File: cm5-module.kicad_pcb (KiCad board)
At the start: 4 copper layers, 100 x 100 mm, 263 parts, among them J1 DIN-41612-connector_090319679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, J10 HDMI-A_HDMI-19PIN-043, J11 USB-C_USB-310F-B-SU, J12 MicroSD_5033981892, J13 Programming connector, J14 Programming connector, J2 JST_SH_1x3_BM03B-SRSS-TB-LF-SN, J3 CM5_1-100_3mm-stack, J4 CM5_101-200_3mm-stack, J5 JST_SH_1x4_BM04B-SRSS-TB-LF-SN, J6 Bus_M.2_1-2199230-6, J7 RJ45_HC612601A-M893-A, J8 USB-A_USB-303WSD-BRY, J9 USB-C_TYPE-C_16PLT-H6.5, Q1 SIS472DN-T1-GE3, Q10 AO3401A, Q11 AO3400A, Q12 AO3400A, Q2 AO3400A, Q3 SIS472DN-T1-GE3, Q4 SIS472DN-T1-GE3, Q5 AO3401A, Q6 AO3401A, Q7 AO3400A, Q8 AO3400A, Q9 AO3401A, SW1 SW_TL2243, U1 LM74700QDBVRQ1, U10 LM74700QDBVRQ1, U11 AP22615AWU-7, U12 LM74700QDBVRQ1, U13 STM32G431CBU6, U14 TJA1044GTK_3Z, U15 STM32G431CBU6, U16 TJA1044GTK_3Z, U17 FSUSB42UMX, U2 AP22615AWU-7, U3 AP22615AWU-7, U4 AP22615AWU-7, U5 FT230XQ-R, U6 NTS0102DP, U7 CH334P, U8 SIC431AED-T1-GE3, U9 TPS564247DRLR, Y1 Oscillator_32.768kHz_OK2EL89C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, Y2 X322512MSB4SI

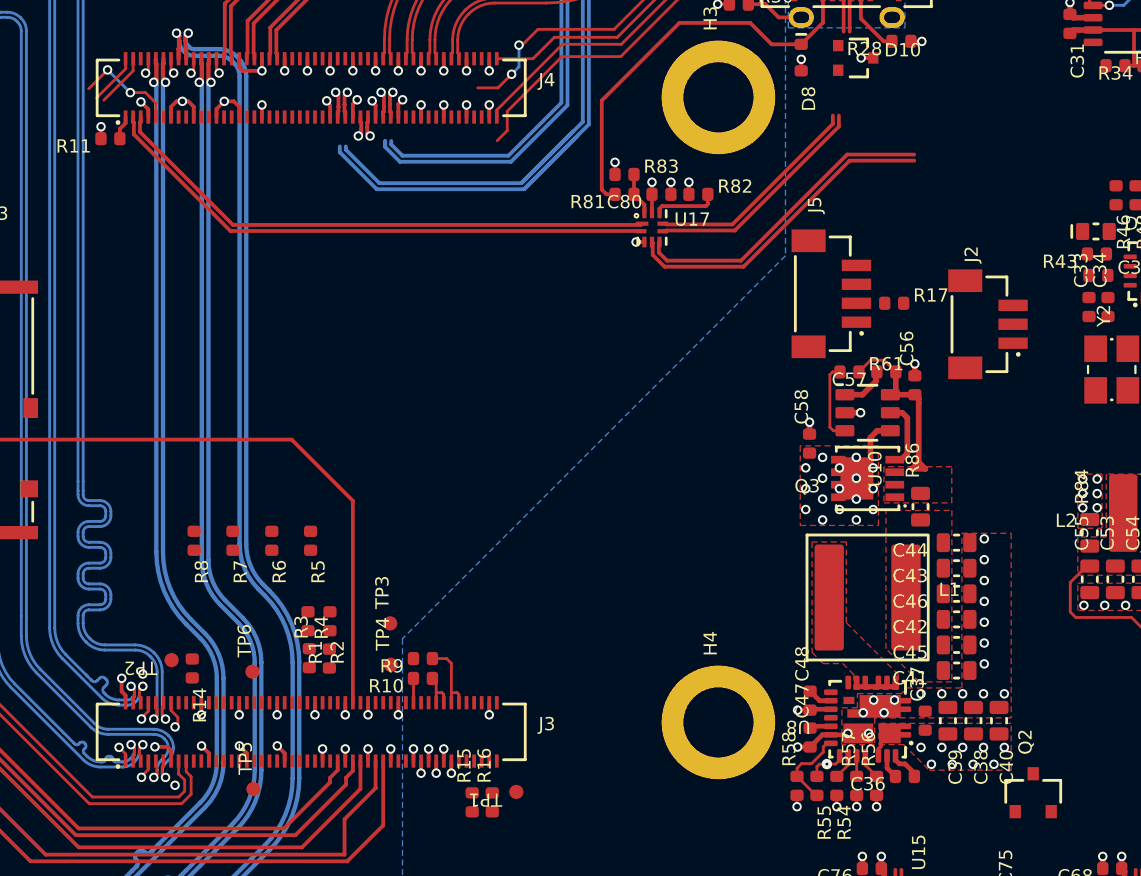
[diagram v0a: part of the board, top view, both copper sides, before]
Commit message: [#3] Move the 5V DC-DC ideal diode, position fan and debug JST connectors
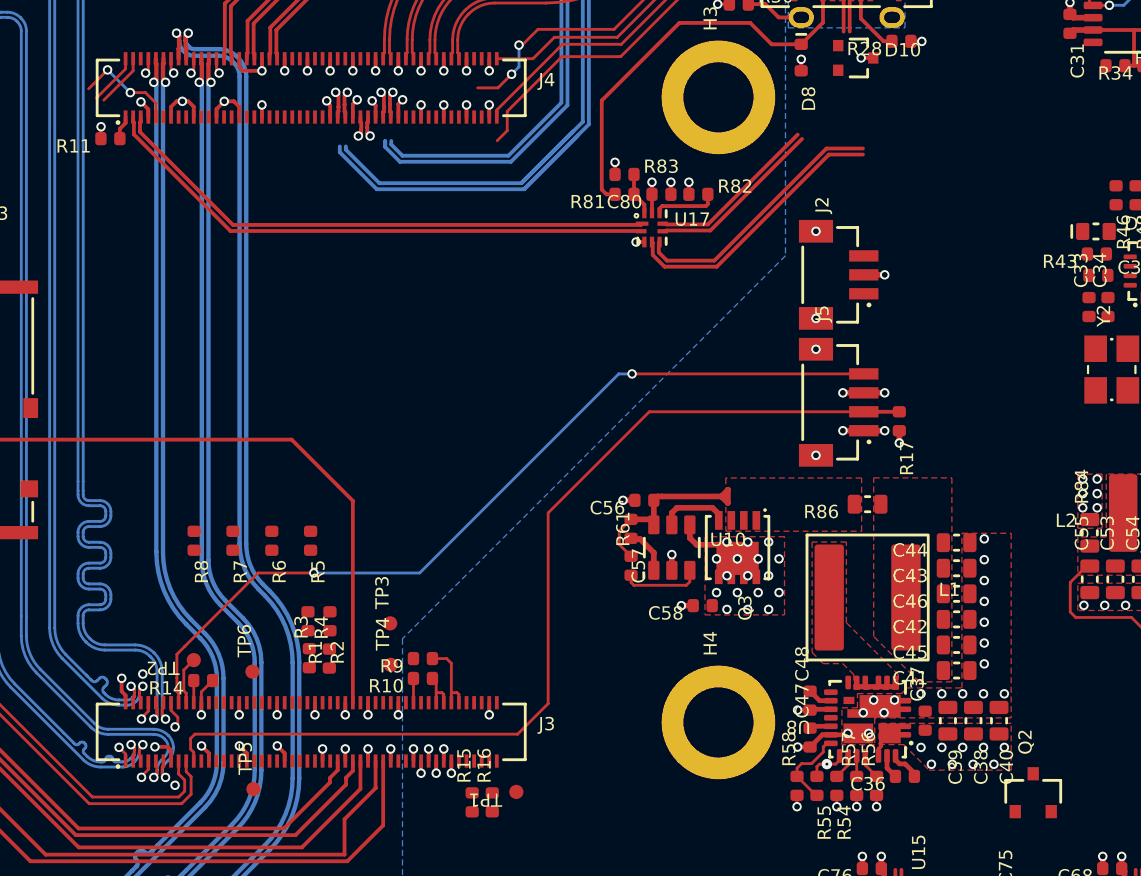
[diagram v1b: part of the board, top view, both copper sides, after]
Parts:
- moved C57 15.8 mm to (90.9, 100.3), turned to -90 degrees
- moved C56 15.5 mm to (91.6, 98.8), turned to 180 degrees
- moved R61 15.4 mm to (90.9, 102.3), turned to 90 degrees
- moved U10 12.6 mm to (93.1, 101.3), turned to 0 degrees
- moved C58 10.2 mm to (94.7, 104.4), turned to 180 degrees
- moved J2 8.30 mm to (101.5, 86.9)
- moved Q3 7.78 mm to (96.6, 101.3), turned to -90 degrees
- moved R17 6.24 mm to (105.1, 94.6), turned to -90 degrees
- moved J5 5.74 mm to (101.5, 93.7)
- moved R86 2.80 mm to (103.4, 99.0), turned to 180 degrees
- moved TP2 1.17 mm to (67.8, 107.3)
- moved R14 0.86 mm to (68.3, 108.3), turned to 180 degrees
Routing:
- net /CM5/FAN_PWM: track 0.00 -> 51.7 mm
- net /CM5/FAN_TACHO: track 0.00 -> 45.0 mm, vias 0 -> 2
- net GND: track 146.9 -> 151.6 mm, vias 204 -> 211
- net /USB switch/USB_2.D-: track 17.7 -> 14.9 mm
- net /USB hub/USB_HUB.D+: track 16.6 -> 14.0 mm
- net /USB hub/USB_HUB.D-: track 17.1 -> 14.5 mm
- net /USB switch/USB_2.D+: track 15.6 -> 13.1 mm
- net Net-(J3-Ethernet_SYNC_OUT): track 0.00 -> 2.52 mm
- net +5V: track 21.1 -> 23.3 mm, vias 50 -> 52
- net /CM5/~{EEPROM_WP}: track 0.00 -> 1.17 mm
- net +3V3: track 40.1 -> 40.8 mm, vias 21 -> 22

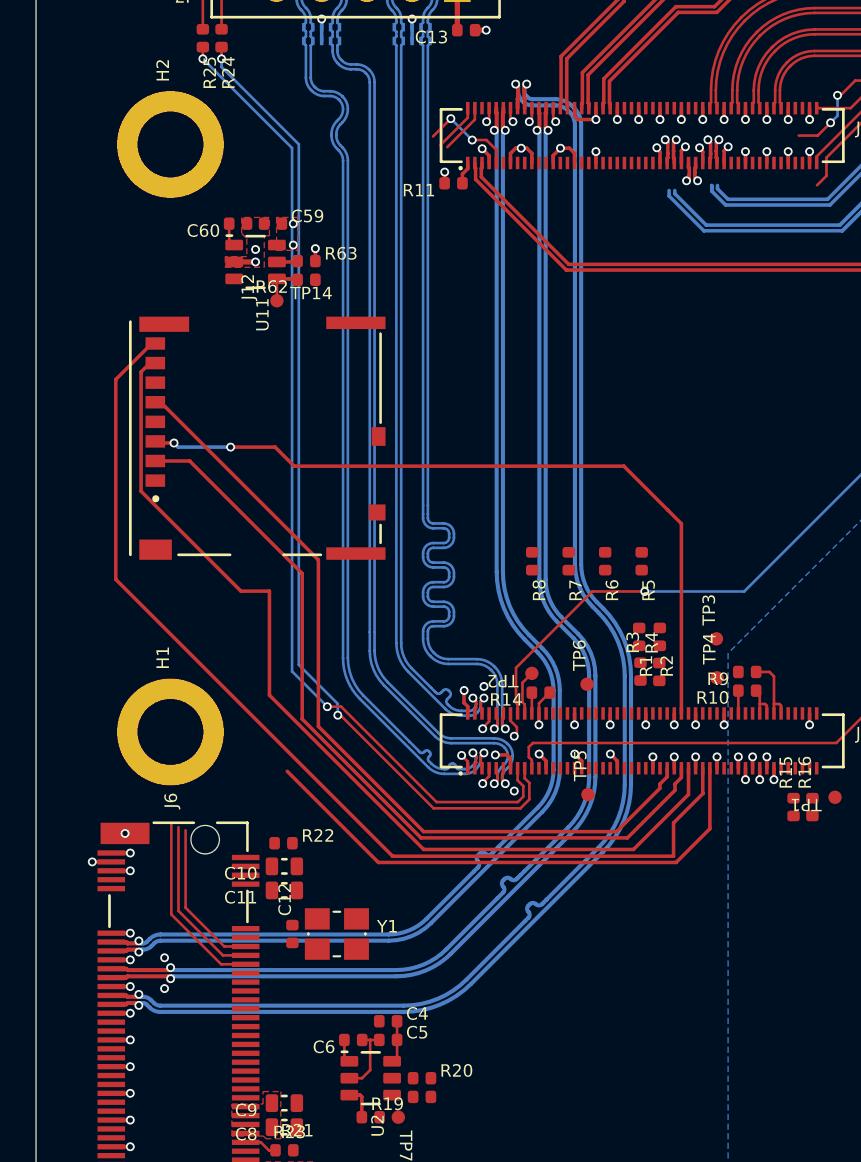
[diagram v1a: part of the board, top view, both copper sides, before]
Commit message: [#3] Layout SD card connector
NOTE: Used 0.3mm traces instead of 0.35mm ones on SDIO lines due to
limited space
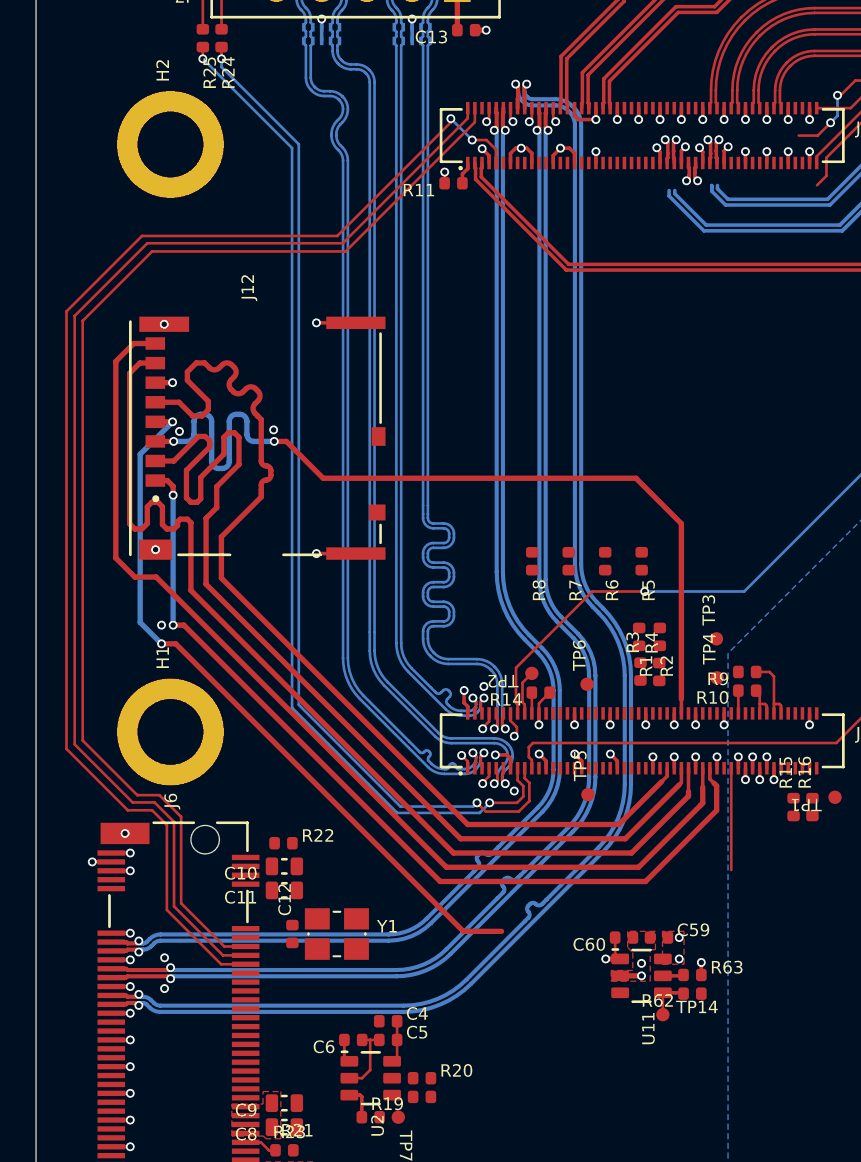
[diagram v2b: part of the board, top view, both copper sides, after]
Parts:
- moved R63 45.6 mm to (76.9, 124.2)
- moved TP14 45.6 mm to (75.2, 126.4)
- moved C60 45.6 mm to (73.0, 122.1)
- moved R62 45.6 mm to (76.9, 125.2)
- moved U11 45.6 mm to (74.0, 124.2)
- moved C59 45.6 mm to (75.0, 122.1)
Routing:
- net /CM5/~{PCIe_PERST}: track 15.9 -> 72.7 mm
- net /CM5/~{PCIe_CLKREQ}: track 12.2 -> 68.6 mm
- net /CM5/~{PCIe_WAKE}: track 11.5 -> 67.8 mm
- net /SD card/SD_+3V3: track 1.32 -> 42.6 mm, vias 0 -> 3
- net /CM5/SD_CARD.DAT2: track 30.0 -> 49.6 mm, vias 0 -> 2
- net /CM5/SD_CARD.DAT3: track 45.2 -> 57.2 mm
- net /CM5/SD_CARD.CLK: track 46.1 -> 57.0 mm
- net /CM5/SD_CARD.CMD: track 42.1 -> 49.8 mm
- net /CM5/SD_PWR_ON: track 0.00 -> 5.72 mm
- net GND: track 151.6 -> 157.0 mm, vias 211 -> 219
- net /CM5/SD_CARD.DAT0: track 53.0 -> 57.3 mm
- net /CM5/ETH.LED_ACT: track 55.0 -> 56.7 mm
- net /CM5/ETH.LED_LINK: track 55.2 -> 56.5 mm

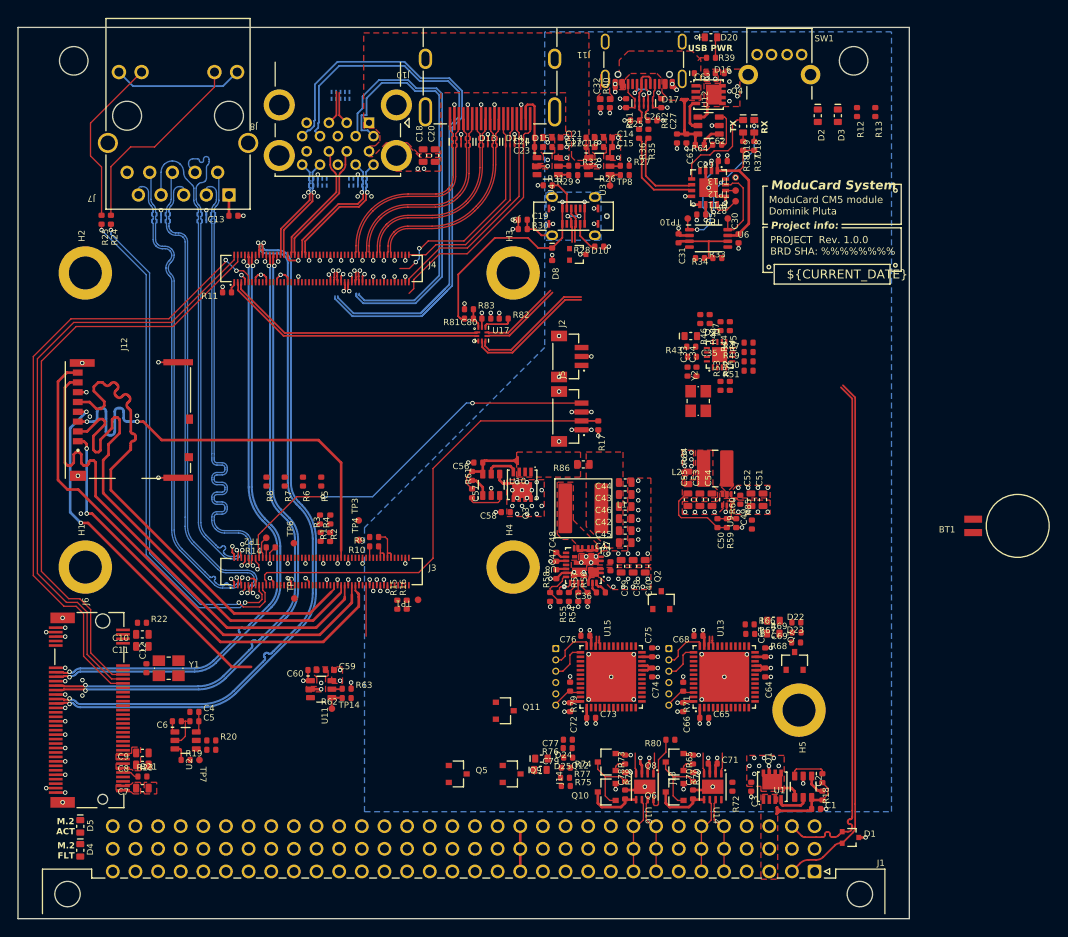
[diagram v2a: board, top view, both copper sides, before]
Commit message: [#3] Layout M.2 power
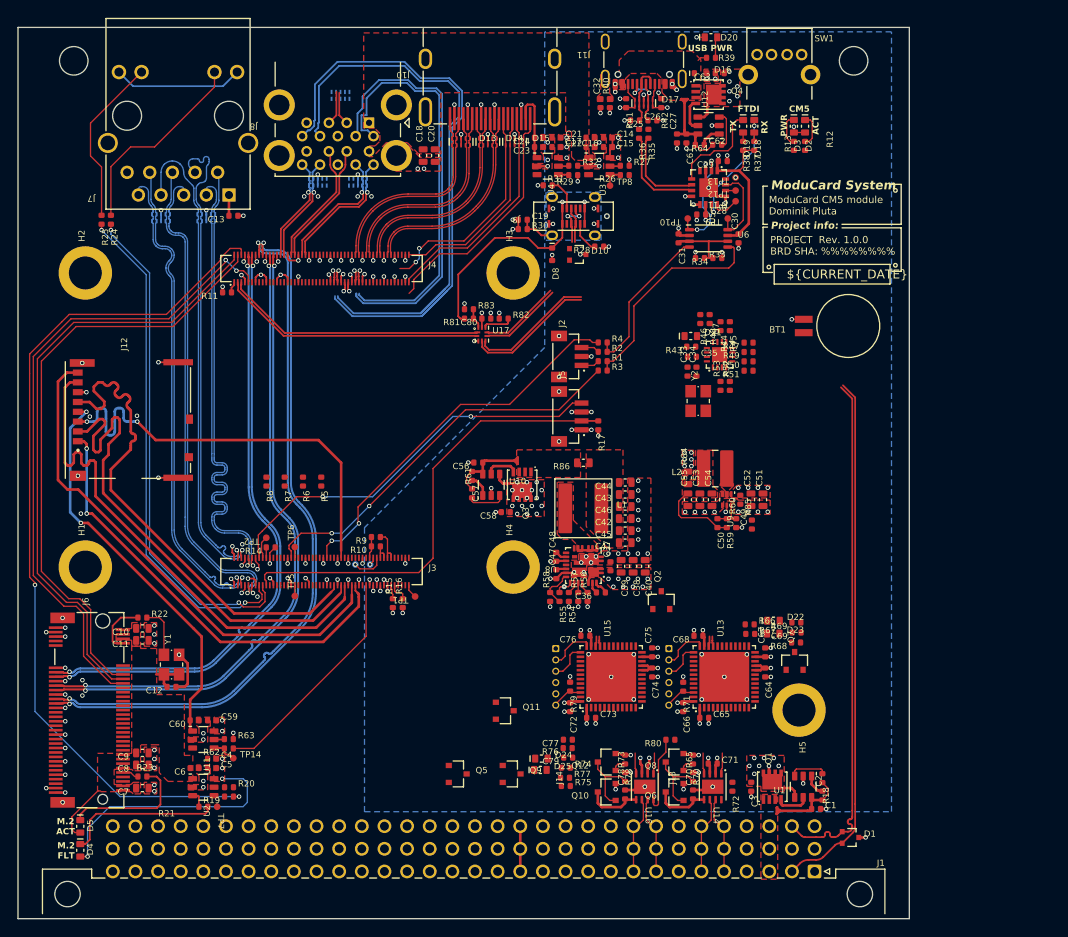
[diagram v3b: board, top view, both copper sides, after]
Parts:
- TP3, TP4: moved to B.Cu
- moved R4 37.6 mm to (105.6, 85.3), turned to 0 degrees
- moved R3 36.7 mm to (105.6, 88.5), turned to 0 degrees
- moved R1 36.4 mm to (105.6, 87.5), turned to 0 degrees
- moved R2 35.9 mm to (105.6, 86.4), turned to 0 degrees
- moved G*** 30.9 mm to (132.7, 79.8)
- moved REF** 30.9 mm to (128.3, 87.0)
- moved BT1 29.4 mm to (128.2, 83.5)
- moved R62 14.4 mm to (63.6, 130.9)
- moved U11 14.4 mm to (60.8, 129.9)
- moved C59 14.4 mm to (61.8, 127.8)
- moved C60 14.4 mm to (59.8, 127.8)
- moved R63 14.4 mm to (63.7, 129.8)
- moved TP14 12.4 mm to (64.1, 132.0)
- moved R13 9.89 mm to (127.0, 63.3), turned to 90 degrees
- moved R12 6.95 mm to (128.3, 63.3), turned to 90 degrees
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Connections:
- net Net-(BT1-+) renamed /CM5/VBAT
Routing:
- net /CM5/PCIe_PWR_EN: track 0.00 -> 97.3 mm, vias 0 -> 2
- net /CM5/UART2_RX: track 0.00 -> 44.3 mm, vias 0 -> 2
- net /CM5/UART2_TX: track 0.00 -> 42.7 mm, vias 0 -> 2
- net +3V3: track 40.8 -> 69.3 mm, vias 22 -> 28
- net /CM5/CONSOLE.TX: track 0.00 -> 24.6 mm
- net /CM5/SD_PWR_ON: track 5.72 -> 25.8 mm
- net Net-(D4-C): track 0.00 -> 17.6 mm
- net /CM5/CONSOLE.RX: track 0.00 -> 17.4 mm
- net Net-(D5-C): track 0.00 -> 14.5 mm
- net +3V3_M2: track 1.32 -> 11.0 mm
- net /M.2/SUSCLK_R: track 0.00 -> 6.22 mm
- net /M.2/SUSCLK: track 0.00 -> 5.79 mm
- net Net-(D2-C): track 0.00 -> 3.68 mm
- net Net-(D3-C): track 0.00 -> 3.66 mm
- net /CM5/SDA0: track 0.00 -> 3.61 mm, vias 0 -> 1
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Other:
- board text added: "ACT"
- board text added: "CM5"
- board text added: "FTDI"
- board text added: "PWR"

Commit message: [#3] Layout USB
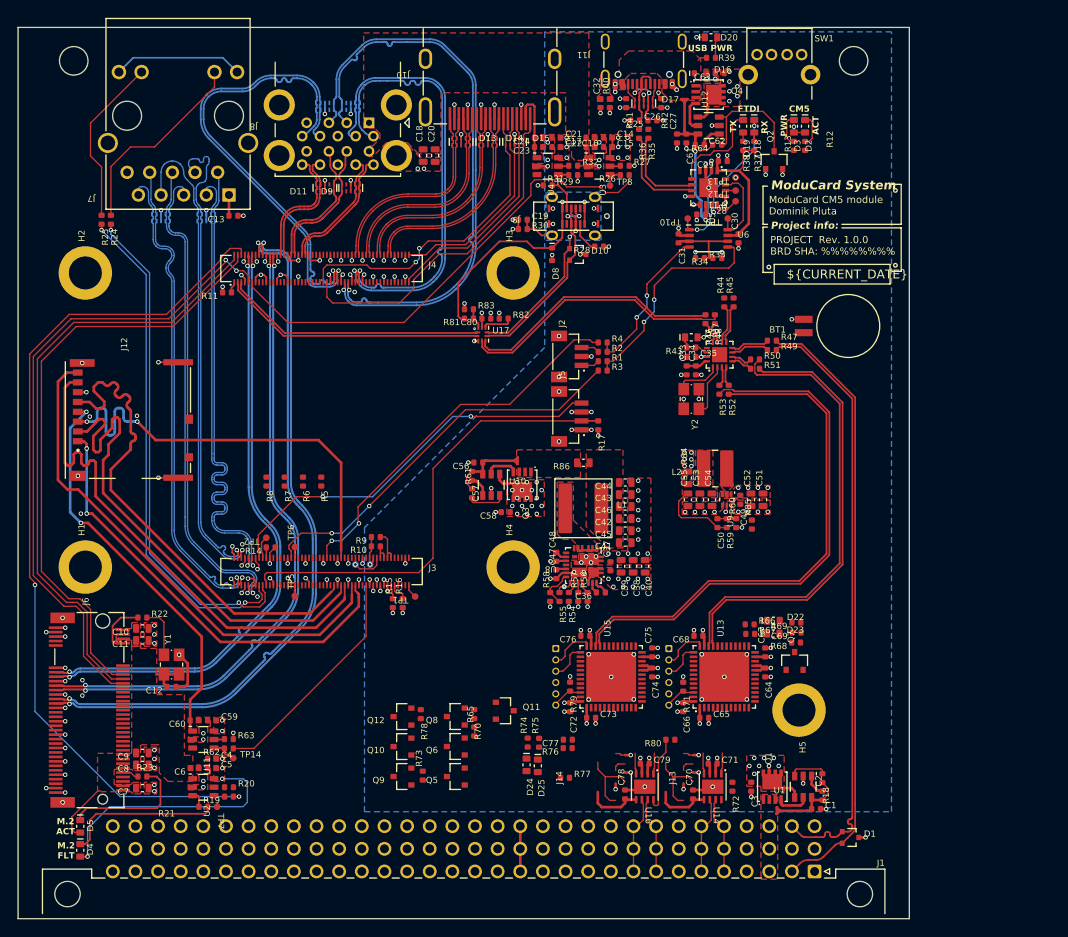
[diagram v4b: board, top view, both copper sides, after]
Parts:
- added D27: PUSB3F96X, DW-footprints:SOT1176-1, B.Cu at (77.3, 58.9)
- D11, D9: moved to F.Cu
- moved Q2 51.0 mm to (124.8, 64.9)
- moved Q8 25.1 mm to (89.1, 127.3)
- moved R65 25.1 mm to (91.2, 129.0)
- moved R70 25.1 mm to (91.2, 127.0)
- moved Q6 25.1 mm to (89.1, 130.7)
- moved Q10 23.5 mm to (83.1, 130.7)
- moved Q12 23.5 mm to (83.1, 127.3)
- moved R78 23.5 mm to (85.2, 127.0)
- moved R73 22.7 mm to (85.4, 133.9)
- moved Q9 12.3 mm to (83.1, 134.1), turned to 180 degrees
- moved C79 8.63 mm to (110.3, 132.6), turned to 0 degrees
- moved R75 5.70 mm to (98.5, 130.3), turned to 90 degrees
- moved R74 5.13 mm to (97.2, 130.2), turned to 90 degrees
- moved R44 2.70 mm to (119.2, 80.9), turned to 90 degrees
- moved R45 2.70 mm to (120.3, 80.9), turned to 90 degrees
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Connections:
- D11 pad 1: unconnected-(D11-CH1-Pad1)_1 -> /CM5/USB_SS_0.D+
- D11 pad 10: unconnected-(D11-CH1-Pad1) -> /CM5/USB_SS_0.D+
- D12 pad 1: /CM5/USB_SS_1.TX+ -> /CM5/USB_SS_1.D+
- D12 pad 10: /CM5/USB_SS_1.TX+ -> /CM5/USB_SS_1.D+
- D12 pad 2: /CM5/USB_SS_1.TX- -> unconnected-(D12-CH2-Pad2)
- D12 pad 9: /CM5/USB_SS_1.TX- -> unconnected-(D12-CH2-Pad2)_1
- D9 pad 5: unconnected-(D9-CH4-Pad5)_1 -> /CM5/USB_SS_0.D-
- D9 pad 6: unconnected-(D9-CH4-Pad5) -> /CM5/USB_SS_0.D-
- R44 pad 2: /CAN to USB 1/USB.D+ -> /USB hub/USB_1.D+
- R45 pad 2: /CAN to USB 1/USB.D- -> /USB hub/USB_1.D-
- R47 pad 2: /CAN to USB 2/USB.D+ -> /Backplane/BACKPLANE.D+
- R49 pad 2: /CAN to USB 2/USB.D- -> /Backplane/BACKPLANE.D-
- R50 pad 2: /Backplane/BACKPLANE.D+ -> /CAN to USB 1/USB.D+
- R51 pad 2: /Backplane/BACKPLANE.D- -> /CAN to USB 1/USB.D-
- R52 pad 2: /USB hub/USB_4.D+ -> /CAN to USB 2/USB.D+
- R53 pad 2: /USB hub/USB_4.D- -> /CAN to USB 2/USB.D-
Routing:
- net /CAN to USB 2/USB.D-: track 1.12 -> 60.5 mm
- net /CM5/USB_SS_1.D-: track 4.79 -> 64.2 mm
- net /CM5/USB_SS_1.D+: track 4.92 -> 64.3 mm
- net /CAN to USB 2/USB.D+: track 1.12 -> 58.6 mm
- net /CM5/VBUS_EN: track 0.00 -> 53.7 mm
- net /CAN to USB 1/USB.D+: track 1.12 -> 51.3 mm
- net /CAN to USB 1/USB.D-: track 1.12 -> 49.6 mm
- net /CM5/USB_SS_1.RX-: track 68.8 -> 52.0 mm
- net /USB hub/USB_HUB.D-: track 14.5 -> 30.9 mm
- net /USB hub/USB_HUB.D+: track 14.0 -> 28.9 mm
- net /CM5/USB_SS_1.RX+: track 66.0 -> 52.1 mm
- net /CM5/HDMI_0.HOTPLUG: track 27.2 -> 38.9 mm
- net /CM5/HDMI_0.CEC: track 24.9 -> 35.8 mm
- net /Backplane/BACKPLANE.D+: track 59.3 -> 68.8 mm
- net /Power/Ideal diode 2/~{DISABLE}: track 4.23 -> 13.7 mm
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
